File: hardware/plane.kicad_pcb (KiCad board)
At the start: 2 copper layers, 32 x 100 mm, 44 parts, among them J1 USB_B_Micro, J2 Conn_Coaxial, J3 Conn_01x03, J4 Conn_01x03, J5 Conn_01x03, J6 Conn_01x03, Q1 BSS138, Q2 BSS138, U1 ESP32-WROOM-32, U2 AMS1117-3.3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

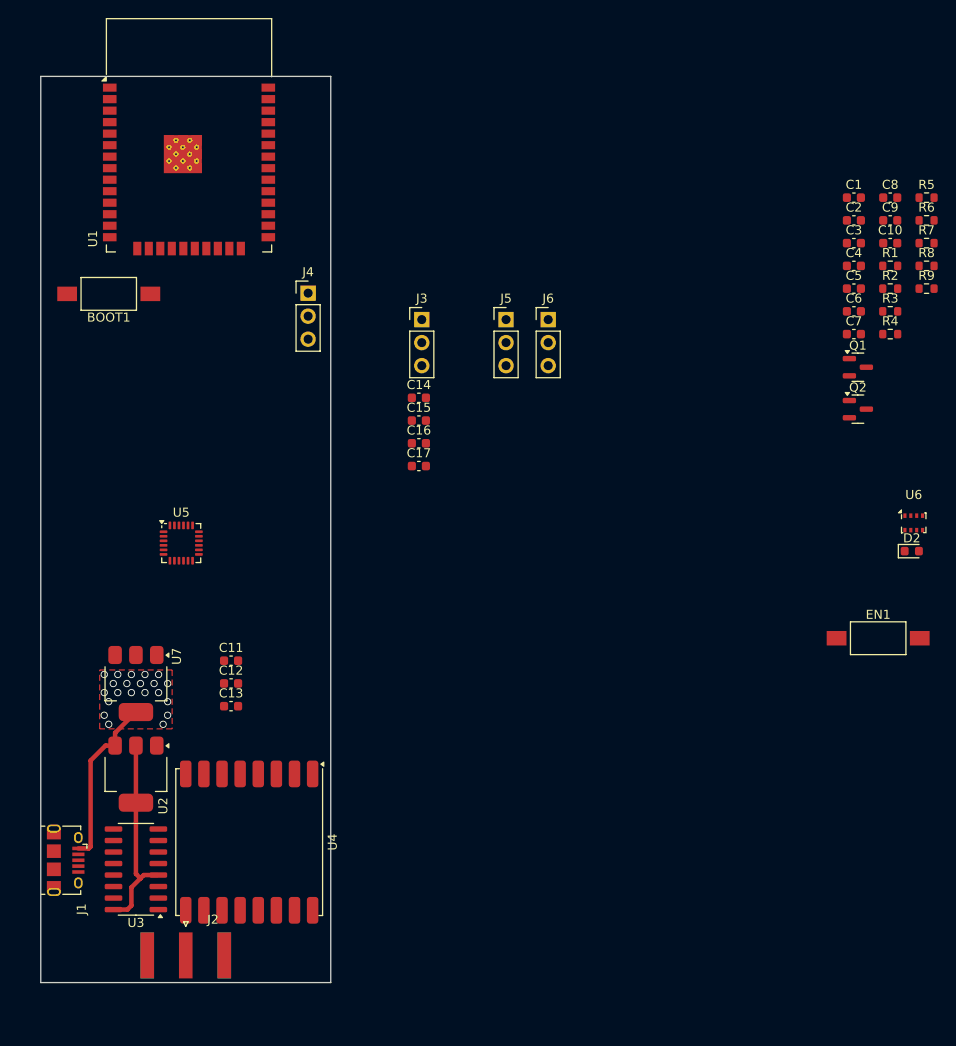
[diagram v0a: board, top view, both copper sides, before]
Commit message: wiring servo
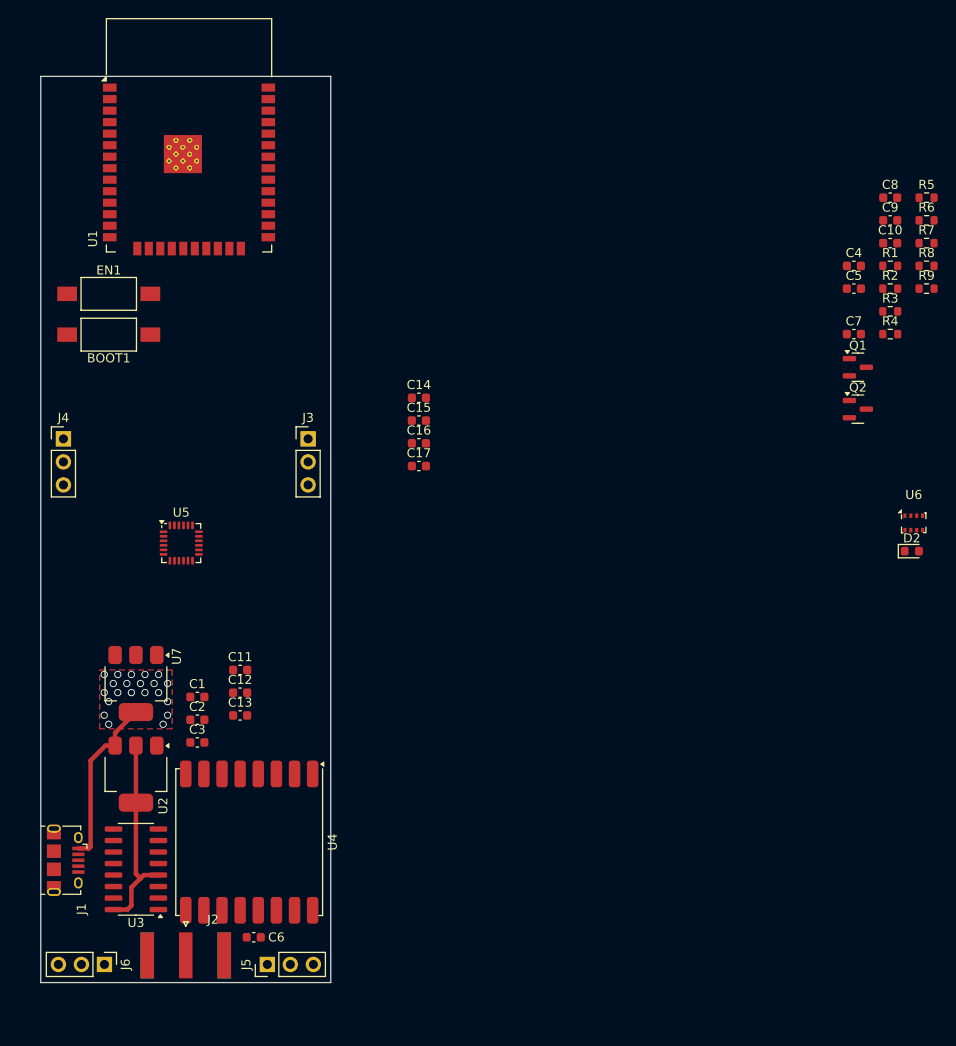
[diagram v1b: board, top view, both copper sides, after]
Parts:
- moved C6 95.7 mm to (123.5, 135.0), turned to 180 degrees
- moved EN1 93.0 mm to (107.5, 64.0)
- moved C1 91.0 mm to (117.3, 108.5)
- moved C2 91.0 mm to (117.3, 111.0)
- moved C3 91.0 mm to (117.3, 113.5)
- moved J6 86.4 mm to (107.0, 138.0), turned to -90 degrees
- moved J5 75.9 mm to (125.0, 138.0), turned to 90 degrees
- moved J4 31.4 mm to (102.5, 80.0)
- moved J3 18.2 mm to (129.5, 80.0)
- moved BOOT1 4.50 mm to (107.5, 68.5)
- moved C12 1.43 mm to (122.0, 108.0)
- moved C11 1.43 mm to (122.0, 105.5)
- moved C13 1.43 mm to (122.0, 110.5)

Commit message: i2c wiring
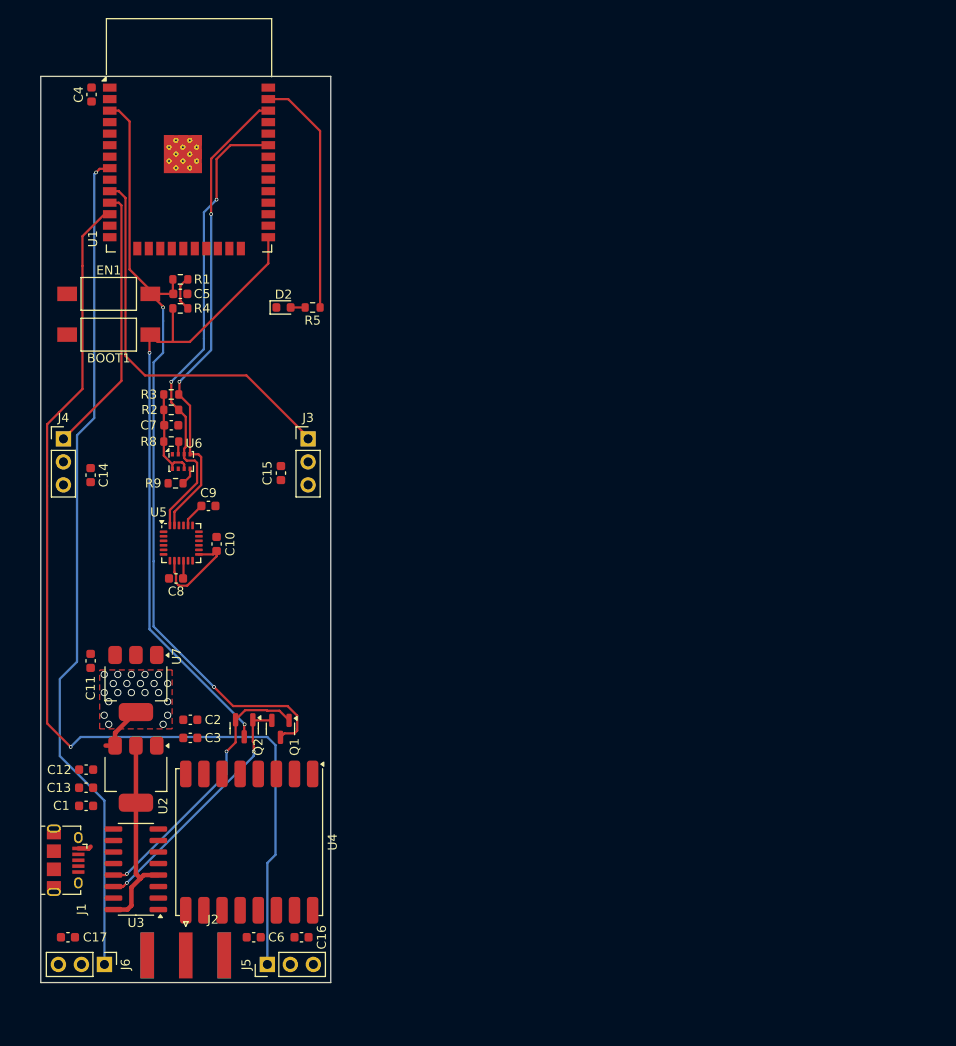
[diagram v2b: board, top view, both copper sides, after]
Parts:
- removed R6, R7: R_Small, Resistor_SMD:R_0603_1608Metric
- U7: value AMS1117-3.3 -> AMS1117-5
- moved C8 89.3 mm to (114.9, 95.4), turned to 180 degrees
- moved C4 86.2 mm to (105.6, 42.0), turned to 90 degrees
- moved R9 85.6 mm to (114.9, 84.9), turned to 180 degrees
- moved R8 85.6 mm to (114.4, 80.3)
- moved C9 81.6 mm to (118.5, 87.4)
- moved C10 81.4 mm to (119.4, 91.6), turned to 90 degrees
- moved U6 81.1 mm to (115.5, 82.5)
- moved R2 80.5 mm to (114.4, 76.8), turned to 180 degrees
- moved R3 79.9 mm to (114.4, 75.1), turned to 180 degrees
- moved R4 78.4 mm to (115.4, 65.6), turned to 180 degrees
- moved R1 78.4 mm to (115.4, 62.4), turned to 180 degrees
- moved Q2 76.3 mm to (122.5, 111.9), turned to -90 degrees
- moved C7 76.0 mm to (114.4, 78.5), turned to 180 degrees
- moved Q1 75.2 mm to (126.5, 112.0), turned to -90 degrees
- moved D2 74.4 mm to (126.8, 65.5)
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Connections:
- C10 pad 1: VCC -> +3V3
- C7 pad 2: VCC -> +3V3
- R8 pad 1: VCC -> +3V3
- U5 pad 13: VCC -> +3V3
- U5 pad 8: VCC -> +3V3
- U6 pad 6: VCC -> +3V3
- U6 pad 8: VCC -> +3V3
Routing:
- net SR3: track 0.00 -> 111.1 mm, vias 0 -> 1
- net SR4: track 0.00 -> 92.8 mm, vias 0 -> 1
- net ESP32_EN: track 0.00 -> 88.3 mm, vias 0 -> 2
- net ESP32_IO0: track 0.00 -> 72.3 mm, vias 0 -> 2
- net SCL: track 0.00 -> 53.2 mm, vias 0 -> 2
- net SDA: track 0.00 -> 51.9 mm, vias 0 -> 2
- net SR1: track 0.00 -> 43.5 mm
- net Net-(Q1-G): track 0.00 -> 30.3 mm, vias 0 -> 2
- net SR2: track 0.00 -> 29.8 mm
- net Net-(Q1-S): track 0.00 -> 27.6 mm, vias 0 -> 2
- net Net-(U1-IO23): track 0.00 -> 26.6 mm
- net +3V3: track 22.6 -> 48.2 mm
- net +5V: track 19.0 -> 7.14 mm
- net Net-(U5-CPOUT): track 0.00 -> 2.76 mm
- net Net-(U5-REGOUT): track 0.00 -> 1.97 mm
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
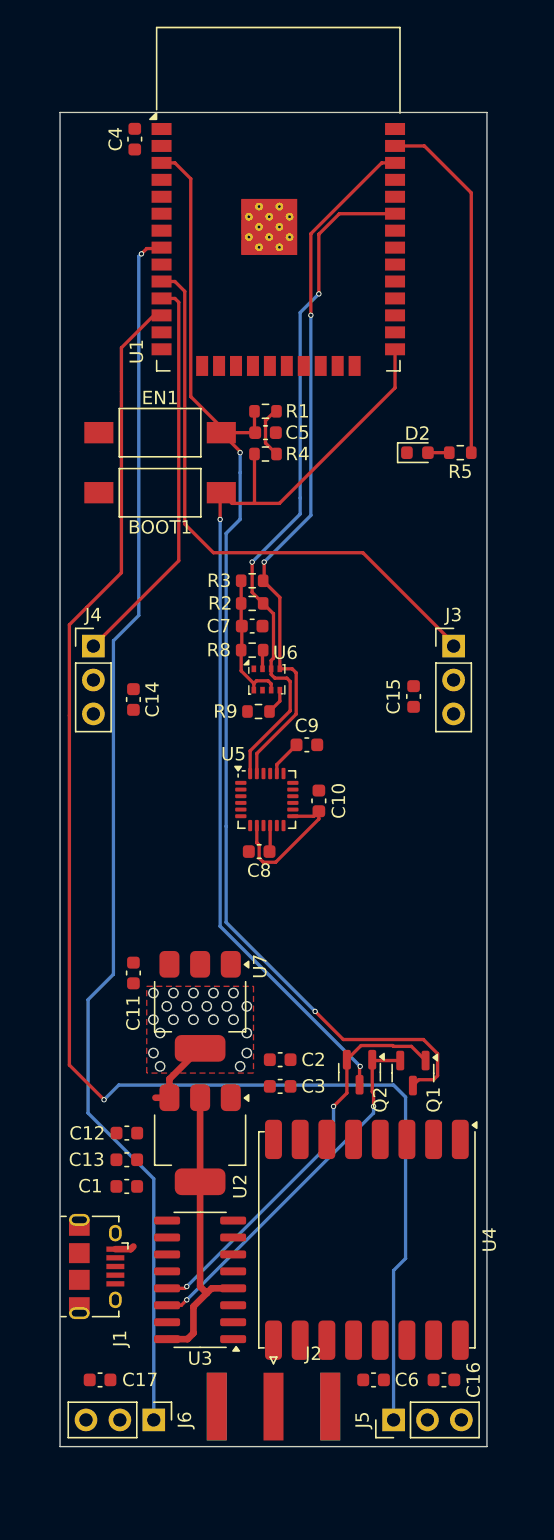
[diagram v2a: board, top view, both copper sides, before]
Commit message: wiring + battery connector
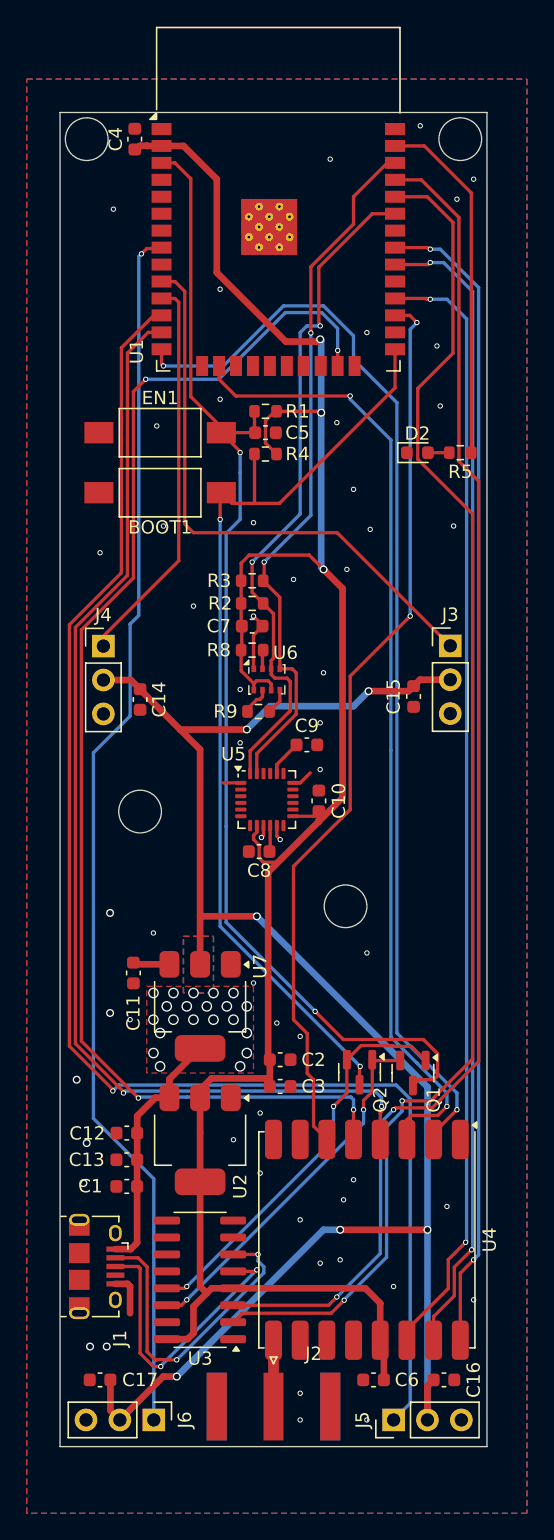
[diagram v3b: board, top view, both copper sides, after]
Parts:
- moved J4 0.75 mm to (103.2, 80.0)
- moved C14 0.50 mm to (106.0, 84.0)
- moved J3 0.25 mm to (129.2, 80.0)
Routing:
- net +5V: track 7.14 -> 149.0 mm, vias 21 -> 27
- net +3V3: track 48.2 -> 162.5 mm, vias 0 -> 3
- net TX-PROG: track 0.00 -> 103.0 mm, vias 0 -> 2
- net RX-PROG: track 0.00 -> 101.5 mm, vias 0 -> 2
- net SS: track 0.00 -> 96.6 mm, vias 0 -> 4
- net DIO2: track 0.00 -> 87.1 mm, vias 0 -> 2
- net DIO1: track 0.00 -> 86.6 mm, vias 0 -> 2
- net SCLK: track 0.00 -> 84.6 mm, vias 0 -> 2
- net DIO0: track 0.00 -> 84.4 mm, vias 0 -> 2
- net MISO: track 0.00 -> 82.5 mm, vias 0 -> 2
- net MOSI: track 0.00 -> 72.5 mm, vias 0 -> 2
- net LORA_RST: track 0.00 -> 68.0 mm, vias 0 -> 2
- net D-: track 0.00 -> 24.2 mm, vias 0 -> 2
- net D+: track 0.00 -> 22.3 mm, vias 0 -> 2
- net GND: track 0.00 -> 14.9 mm, vias 0 -> 56
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- added copper zone on B.Cu, net +5V
- added copper zone on B.Cu, net GND
- added copper zone on F.Cu, net GND
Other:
- outline, holes or cut-outs redrawn

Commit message: pcb battery connector
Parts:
- added J7: Conn_01x02, Connector_AMASS:AMASS_XT30U-F_1x02_P5.0mm_Vertical, F.Cu at (106.5, 91.5)
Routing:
- net +BATT: track 2.75 -> 11.0 mm
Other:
- outline, holes or cut-outs redrawn

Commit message: add esc connector
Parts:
- added BATT: TestPoint, TestPoint:TestPoint_Pad_2.5x2.5mm, F.Cu at (103.0, 55.0)
- added GND: TestPoint, TestPoint:TestPoint_Pad_2.5x2.5mm, F.Cu at (103.0, 46.0)
- added PWM: TestPoint, TestPoint:TestPoint_Pad_2.5x2.5mm, F.Cu at (103.0, 50.5)
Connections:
- U1 pad 9: unconnected-(U1-IO33-Pad9) -> MOTOR
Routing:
- net +BATT: track 11.0 -> 57.6 mm, vias 0 -> 1
- net SR4: track 92.5 -> 99.9 mm
- net MOTOR: track 0.00 -> 4.98 mm
- net GND: vias 56 -> 66
